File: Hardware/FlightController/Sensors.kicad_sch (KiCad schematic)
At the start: 0 parts

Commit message: Add ICM-42670-P symbol and schematic
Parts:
- added C18: 10nF, Capacitor_SMD:C_0603_1608Metric, symbol Device:C_Small
- added C19: 0.1uF, Capacitor_SMD:C_0603_1608Metric, symbol Device:C_Small
- added C20: 2.2uF, Capacitor_SMD:C_0603_1608Metric, symbol Device:C_Small
- added U4: ICM-42670-P, Package_LGA:LGA-14_3x2.5mm_P0.5mm_LayoutBorder3x4y, symbol FlightControllerLibrary:ICM-42670-P
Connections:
- new net +3V3: C18.1, C19.1, C20.1, U4.12 (AP_CS), U4.5 (VDDIO), U4.8 (VDD)
- new net GND: C18.2, C19.2, C20.2, U4.6 (GND)
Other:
- note added: "IMU"
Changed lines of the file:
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@@
 (kicad_sch (version 20211123) (generator eeschema)
   (paper "A4")
+  (junction (at 90.17 55.88) (diameter 0) (color 0 0 0 0)
+  )
+  (junction (at 77.47 55.88) (diameter 0) (color 0 0 0 0)
+  )
+  (wire (pts (xy 35.56 76.2) (xy 35.56 80.01))
+    (stroke (width 0) (type default) (color 0 0 0 0))
+  )
+  (polyline (pts (xy 16.51 22.86) (xy 110.49 22.86))
+    (stroke (width 0) (type default) (color 0 0 0 0))
+  )
+  (wire (pts (xy 22.86 67.31) (xy 35.56 67.31))
+    (stroke (width 0) (type default) (color 0 0 0 0))
+  )
+  (wire (pts (xy 72.39 55.88) (xy 77.47 55.88))
+    (stroke (width 0) (type default) (color 0 0 0 0))
+  )
+  (wire (pts (xy 77.47 55.88) (xy 90.17 55.88))
+    (stroke (width 0) (type default) (color 0 0 0 0))
+  )
+  (wire (pts (xy 90.17 55.88) (xy 97.79 55.88))
+    (stroke (width 0) (type default) (color 0 0 0 0))
+  )
+  (polyline (pts (xy 110.49 22.86) (xy 110.49 87.63))
+    (stroke (width 0) (type default) (color 0 0 0 0))
+  )
+  (wire (pts (xy 35.56 67.31) (xy 35.56 71.12))
+    (stroke (width 0) (type default) (color 0 0 0 0))
+  )
+  (polyline (pts (xy 16.51 87.63) (xy 16.51 22.86))
+    (stroke (width 0) (type default) (color 0 0 0 0))
+  )
+  (polyline (pts (xy 110.49 87.63) (xy 16.51 87.63))
+    (stroke (width 0) (type default) (color 0 0 0 0))
+  )
+  (text "IMU" (at 58.42 21.59 0)
+    (effects (font (size 1.27 1.27) (thickness 0.254) bold) (justify left bottom))
+  )
+  (global_label "ACCEL_VDDIO" (shape input) (at 60.96 40.64 90) (fields_autoplaced)
+    (effects (font (size 1.27 1.27)) (justify left))
+    (property "Intersheet References" "${INTERSHEET_REFS}" (id 0) (at 61.0394 25.8898 90)
+      (effects (font (size 1.27 1.27)) (justify left) hide)
+    )
+  )
+  (global_label "ACCEL_VDDIO" (shape input) (at 35.56 67.31 0) (fields_autoplaced)
+    (effects (font (size 1.27 1.27)) (justify left))
+    (property "Intersheet References" "${INTERSHEET_REFS}" (id 0) (at 50.3102 67.3894 0)
+      (effects (font (size 1.27 1.27)) (justify left) hide)
+    )
+  )
+  (global_label "ACCEL_VDDIO" (shape input) (at 55.88 59.69 270) (fields_autoplaced)
+    (effects (font (size 1.27 1.27)) (justify right))
+    (property "Intersheet References" "${INTERSHEET_REFS}" (id 0) (at 55.8006 74.4402 90)
+      (effects (font (size 1.27 1.27)) (justify right) hide)
+    )
+  )
+  (symbol (lib_id "power:GND") (at 90.17 60.96 0) (unit 1)
+    (in_bom yes) (on_board yes) (fields_autoplaced)
+    (property "Reference" "#PWR026" (id 0) (at 90.17 67.31 0)
+      (effects (font (size 1.27 1.27)) hide)
+    )
+    (property "Value" "GND" (id 1) (at 90.17 66.04 0))
+    (property "Footprint" "" (id 2) (at 90.17 60.96 0)
+      (effects (font (size 1.27 1.27)) hide)
+    )
+    (property "Datasheet" "" (id 3) (at 90.17 60.96 0)
+      (effects (font (size 1.27 1.27)) hide)
+    )
+    (pin "1")
+  )
+  (symbol (lib_id "power:GND") (at 77.47 60.96 0) (unit 1)
+    (in_bom yes) (on_board yes) (fields_autoplaced)
+    (property "Reference" "#PWR025" (id 0) (at 77.47 67.31 0)
+      (effects (font (size 1.27 1.27)) hide)
+    )
+    (property "Value" "GND" (id 1) (at 77.47 66.04 0))
+    (property "Footprint" "" (id 2) (at 77.47 60.96 0)
+      (effects (font (size 1.27 1.27)) hide)
+    )
+    (property "Datasheet" "" (id 3) (at 77.47 60.96 0)
+      (effects (font (size 1.27 1.27)) hide)
+    )
+    (pin "1")
+  )
+  (symbol (lib_id "power:GND") (at 35.56 80.01 0) (unit 1)
+    (in_bom yes) (on_board yes) (fields_autoplaced)
+    (property "Reference" "#PWR023" (id 0) (at 35.56 86.36 0)
+      (effects (font (size 1.27 1.27)) hide)
+    )
+    (property "Value" "GND" (id 1) (at 35.56 85.09 0))
+    (property "Footprint" "" (id 2) (at 35.56 80.01 0)
+      (effects (font (size 1.27 1.27)) hide)
+    )
+    (property "Datasheet" "" (id 3) (at 35.56 80.01 0)
+      (effects (font (size 1.27 1.27)) hide)
+    )
+    (pin "1")
+  )
+  (symbol (lib_id "Device:C_Small") (at 35.56 73.66 0) (unit 1)
+    (in_bom yes) (on_board yes) (fields_autoplaced)
+    (property "Reference" "C18" (id 0) (at 38.1 72.3962 0)
+      (effects (font (size 1.27 1.27)) (justify left))
+    )
+    (property "Value" "10nF" (id 1) (at 38.1 74.9362 0)
+      (effects (font (size 1.27 1.27)) (justify left))
+    )
+    (property "Footprint" "Capacitor_SMD:C_0603_1608Metric" (id 2) (at 35.56 73.66 0)
+      (effects (font (size 1.27 1.27)) hide)
+    )
+    (property "Datasheet" "~" (id 3) (at 35.56 73.66 0)
+      (effects (font (size 1.27 1.27)) hide)
+    )
+    (pin "1")
+    (pin "2")
+  )
+  (symbol (lib_id "power:GND") (at 58.42 59.69 0) (unit 1)
+    (in_bom yes) (on_board yes) (fields_autoplaced)
+    (property "Reference" "#PWR024" (id 0) (at 58.42 66.04 0)
+      (effects (font (size 1.27 1.27)) hide)
+    )
+    (property "Value" "GND" (id 1) (at 58.42 64.77 0))
+    (property "Footprint" "" (id 2) (at 58.42 59.69 0)
+      (effects (font (size 1.27 1.27)) hide)
+    )
+    (property "Datasheet" "" (id 3) (at 58.42 59.69 0)
+      (effects (font (size 1.27 1.27)) hide)
+    )
+    (pin "1")
+  )
+  (symbol (lib_id "power:+3.3V") (at 22.86 67.31 90) (unit 1)
+    (in_bom yes) (on_board yes)
+    (property "Reference" "#PWR022" (id 0) (at 26.67 67.31 0)
+      (effects (font (size 1.27 1.27)) hide)
+    )
+    (property "Value" "+3.3V" (id 1) (at 21.59 64.77 90)
+      (effects (font (size 1.27 1.27)) (justify right))
+    )
+    (property "Footprint" "" (id 2) (at 22.86 67.31 0)
+      (effects (font (size 1.27 1.27)) hide)
+    )
+    (property "Datasheet" "" (id 3) (at 22.86 67.31 0)
+      (effects (font (size 1.27 1.27)) hide)
+    )
+    (pin "1")
+  )
+  (symbol (lib_id "Device:C_Small") (at 77.47 58.42 0) (unit 1)
+    (in_bom yes) (on_board yes) (fields_autoplaced)
+    (property "Reference" "C19" (id 0) (at 80.01 57.1562 0)
+      (effects (font (size 1.27 1.27)) (justify left))
+    )
+    (property "Value" "0.1uF" (id 1) (at 80.01 59.6962 0)
+      (effects (font (size 1.27 1.27)) (justify left))
+    )
+    (property "Footprint" "Capacitor_SMD:C_0603_1608Metric" (id 2) (at 77.47 58.42 0)
+      (effects (font (size 1.27 1.27)) hide)
+    )
+    (property "Datasheet" "~" (id 3) (at 77.47 58.42 0)
+      (effects (font (size 1.27 1.27)) hide)
+    )
+    (pin "1")
+    (pin "2")
+  )
+  (symbol (lib_id "FlightControllerLibrary:ICM-42670-P") (at 55.88 48.26 0) (unit 1)
+    (in_bom yes) (on_board yes) (fields_autoplaced)
+    (property "Reference" "U4" (id 0) (at 62.9794 38.1 0)
+      (effects (font (size 1.27 1.27)) (justify left))
+    )
+    (property "Value" "ICM-42670-P" (id 1) (at 62.9794 40.64 0)
+      (effects (font (size 1.27 1.27)) (justify left))
+    )
+    (property "Footprint" "Package_LGA:LGA-14_3x2.5mm_P0.5mm_LayoutBorder3x4y" (id 2) (at 55.88 45.72 0)
+      (effects (font (size 1.27 1.27)) hide)
+    )
+    (property "Datasheet" "" (id 3) (at 55.88 45.72 0)
+      (effects (font (size 1.27 1.27)) hide)
+    )
+    (pin "1")
+    (pin "10")
+    (pin "11")
+    (pin "12")
+    (pin "13")
+    (pin "14")
+    (pin "2")
+    (pin "3")
+    (pin "4")
+    (pin "5")
+    (pin "6")
+    (pin "7")
+    (pin "8")
+    (pin "9")
+  )
+  (symbol (lib_id "Device:C_Small") (at 90.17 58.42 0) (unit 1)
+    (in_bom yes) (on_board yes) (fields_autoplaced)
+    (property "Reference" "C20" (id 0) (at 92.71 57.1562 0)
+      (effects (font (size 1.27 1.27)) (justify left))
+    )
+    (property "Value" "2.2uF" (id 1) (at 92.71 59.6962 0)
+      (effects (font (size 1.27 1.27)) (justify left))
+    )
+    (property "Footprint" "Capacitor_SMD:C_0603_1608Metric" (id 2) (at 90.17 58.42 0)
+      (effects (font (size 1.27 1.27)) hide)
+    )
+    (property "Datasheet" "~" (id 3) (at 90.17 58.42 0)
+      (effects (font (size 1.27 1.27)) hide)
+    )
+    (pin "1")
+    (pin "2")
+  )
+  (symbol (lib_id "power:+3.3V") (at 97.79 55.88 270) (unit 1)
+    (in_bom yes) (on_board yes) (fields_autoplaced)
+    (property "Reference" "#PWR027" (id 0) (at 93.98 55.88 0)
+      (effects (font (size 1.27 1.27)) hide)
+    )
+    (property "Value" "+3.3V" (id 1) (at 101.6 55.8799 90)
+      (effects (font (size 1.27 1.27)) (justify left))
+    )
+    (property "Footprint" "" (id 2) (at 97.79 55.88 0)
+      (effects (font (size 1.27 1.27)) hide)
+    )
+    (property "Datasheet" "" (id 3) (at 97.79 55.88 0)
+      (effects (font (size 1.27 1.27)) hide)
+    )
+    (pin "1")
+  )
 )

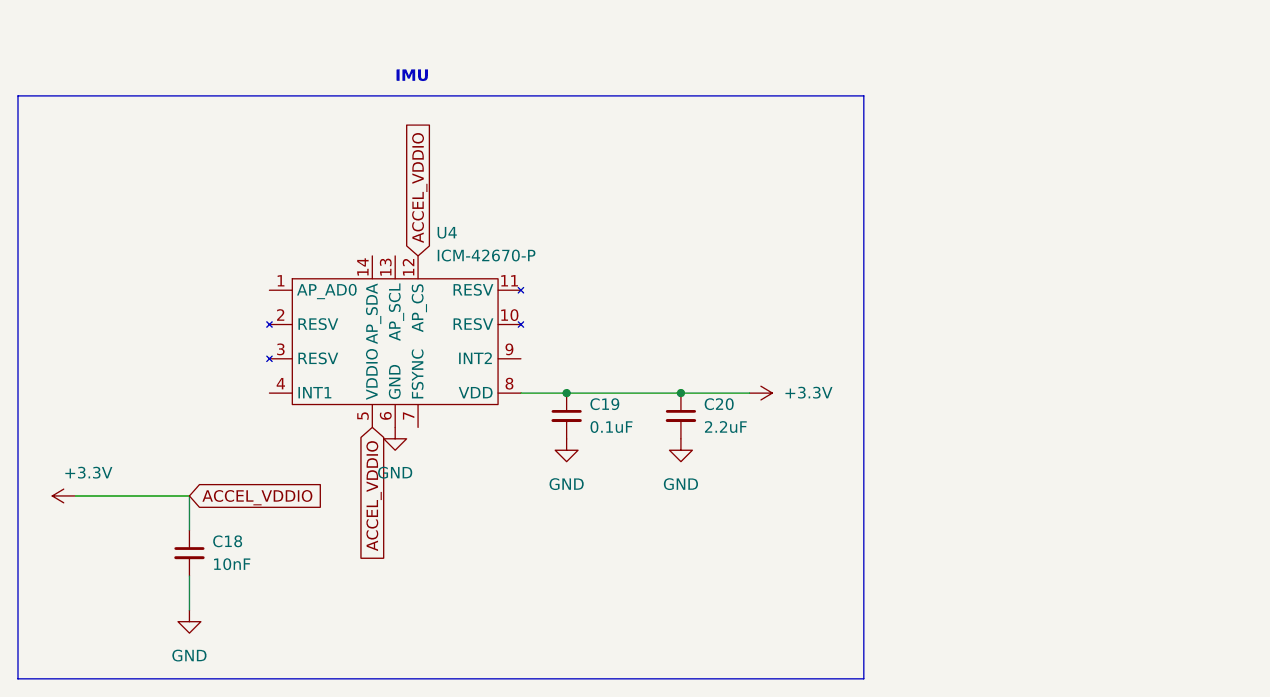
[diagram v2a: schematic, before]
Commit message: Round out basic schematic and add preliminary board layout
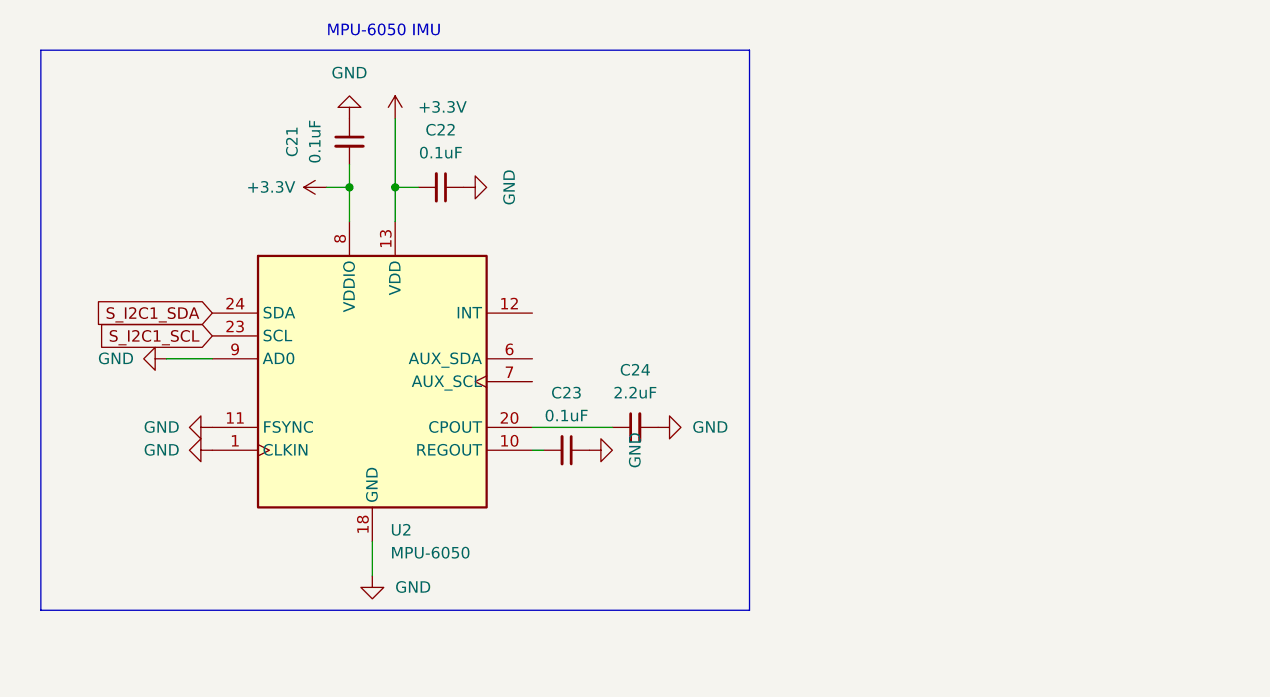
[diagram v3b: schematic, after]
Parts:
- removed C18: 10nF, Capacitor_SMD:C_0603_1608Metric, symbol Device:C_Small
- removed C19: 0.1uF, Capacitor_SMD:C_0603_1608Metric, symbol Device:C_Small
- removed C20: 2.2uF, Capacitor_SMD:C_0603_1608Metric, symbol Device:C_Small
- removed U4: ICM-42670-P, Package_LGA:LGA-14_3x2.5mm_P0.5mm_LayoutBorder3x4y, symbol FlightControllerLibrary:ICM-42670-P
- added C21, C22, C23: 0.1uF, Capacitor_SMD:C_0402_1005Metric, symbol Device:C_Small
- added C24: 2.2uF, Capacitor_SMD:C_0402_1005Metric, symbol Device:C_Small
- added U2: MPU-6050, Sensor_Motion:InvenSense_QFN-24_4x4mm_P0.5mm, symbol Sensor_Motion:MPU-6050
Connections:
- net +3V3: now also C21.2, C22.2, U2.13 (VDD), U2.8 (VDDIO)
- net GND: now also C21.1, C22.1, C23.1, C24.2, U2.1 (CLKIN), U2.11 (FSYNC), U2.18 (GND), U2.9 (AD0)
- new net: C24.1, U2.20 (CPOUT)
- new net: C23.2, U2.10 (REGOUT)
- new net S_I2C1_SCL: U2.23 (SCL)
- new net S_I2C1_SDA: U2.24 (SDA)
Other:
- note added: "MPU-6050 IMU"
- note removed: "IMU"

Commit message: Add and route SBUS inverter
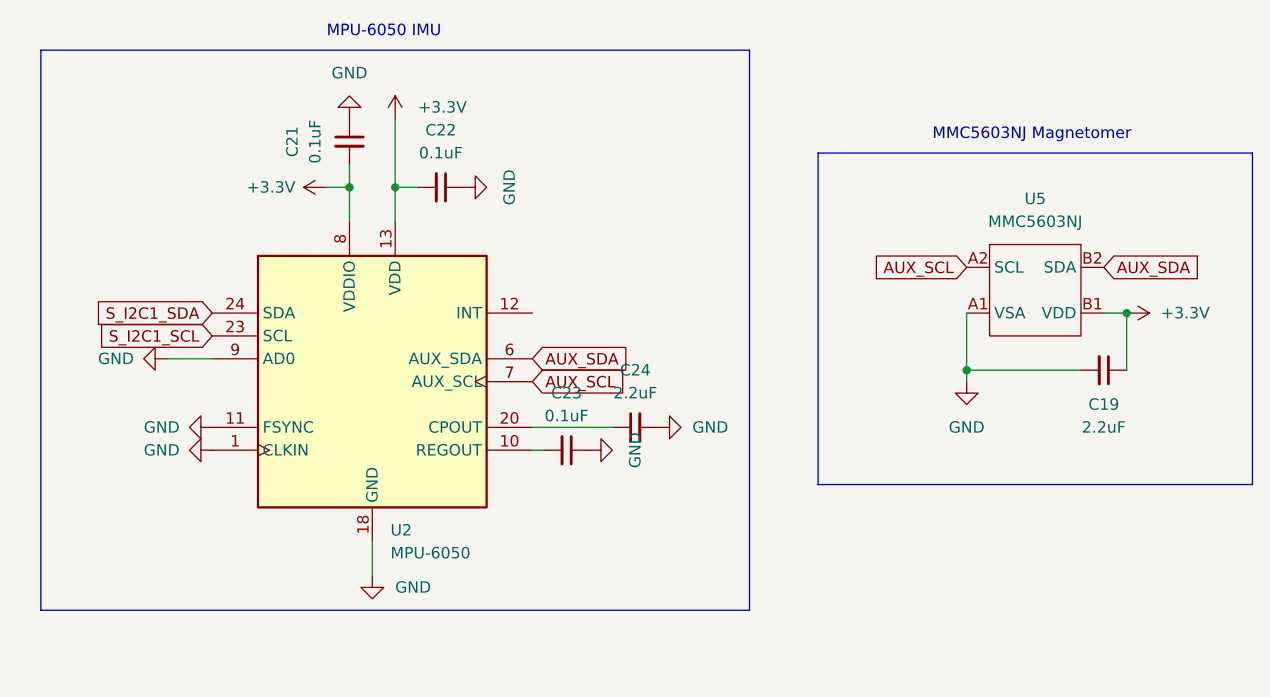
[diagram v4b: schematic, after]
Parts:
- added C19: 2.2uF, Capacitor_SMD:C_0402_1005Metric, symbol Device:C_Small
- added U5: MMC5603NJ, Package_BGA:WLP-4_0.83x0.83mm_P0.4mm, symbol FlightControllerLibrary:MMC5603NJ
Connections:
- net +3V3: now also C19.1, U5.B1 (VDD)
- net GND: now also C19.2, U5.A1 (VSA)
- net AUX_SDA: now reaches U2.6 (AUX_SDA)
- net AUX_SDA: now also U5.B2 (SDA)
- net AUX_SCL: now reaches U2.7 (AUX_SCL)
- net AUX_SCL: now also U5.A2 (SCL)
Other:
- note added: "MMC5603NJ Magnetomer"
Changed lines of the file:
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@@
   (junction (at 58.42 33.02) (diameter 0) (color 0 0 0 0)
   )
+  (junction (at 121.92 53.34) (diameter 0) (color 0 0 0 0)
+  )
   (junction (at 53.34 33.02) (diameter 0) (color 0 0 0 0)
   )
+  (junction (at 139.7 46.99) (diameter 0) (color 0 0 0 0)
+  )
   (polyline (pts (xy 19.05 80.01) (xy 19.05 17.78))
     (stroke (width 0) (type default) (color 0 0 0 0))
@@
     (stroke (width 0) (type default) (color 0 0 0 0))
   )
+  (wire (pts (xy 121.92 53.34) (xy 134.62 53.34))
+    (stroke (width 0) (type default) (color 0 0 0 0))
+  )
+  (polyline (pts (xy 153.67 66.04) (xy 105.41 66.04))
+    (stroke (width 0) (type default) (color 0 0 0 0))
+  )
+  (polyline (pts (xy 105.41 66.04) (xy 105.41 29.21))
+    (stroke (width 0) (type default) (color 0 0 0 0))
+  )
   (wire (pts (xy 53.34 33.02) (xy 53.34 36.83))
     (stroke (width 0) (type default) (color 0 0 0 0))
   )
+  (wire (pts (xy 137.16 46.99) (xy 139.7 46.99))
+    (stroke (width 0) (type default) (color 0 0 0 0))
+  )
   (wire (pts (xy 55.88 76.2) (xy 55.88 72.39))
     (stroke (width 0) (type default) (color 0 0 0 0))
@@
     (stroke (width 0) (type default) (color 0 0 0 0))
   )
+  (wire (pts (xy 121.92 53.34) (xy 121.92 54.61))
+    (stroke (width 0) (type default) (color 0 0 0 0))
+  )
   (polyline (pts (xy 97.79 80.01) (xy 19.05 80.01))
     (stroke (width 0) (type default) (color 0 0 0 0))
   )
+  (polyline (pts (xy 153.67 29.21) (xy 153.67 66.04))
+    (stroke (width 0) (type default) (color 0 0 0 0))
+  )
+  (wire (pts (xy 139.7 46.99) (xy 139.7 53.34))
+    (stroke (width 0) (type default) (color 0 0 0 0))
+  )
   (wire (pts (xy 58.42 33.02) (xy 58.42 36.83))
     (stroke (width 0) (type default) (color 0 0 0 0))
   )
+  (wire (pts (xy 121.92 46.99) (xy 121.92 53.34))
+    (stroke (width 0) (type default) (color 0 0 0 0))
+  )
   (polyline (pts (xy 97.79 17.78) (xy 97.79 80.01))
     (stroke (width 0) (type default) (color 0 0 0 0))
@@
     (stroke (width 0) (type default) (color 0 0 0 0))
   )
+  (polyline (pts (xy 105.41 29.21) (xy 153.67 29.21))
+    (stroke (width 0) (type default) (color 0 0 0 0))
+  )
   (text "MPU-6050 IMU" (at 50.8 16.51 0)
+    (effects (font (size 1.27 1.27)) (justify left bottom))
+  )
+  (text "MMC5603NJ Magnetomer" (at 118.11 27.94 0)
     (effects (font (size 1.27 1.27)) (justify left bottom))
   )
@@
     )
   )
+  (global_label "AUX_SCL" (shape input) (at 73.66 54.61 0) (fields_autoplaced)
+    (effects (font (size 1.27 1.27)) (justify left))
+    (property "Intersheet References" "${INTERSHEET_REFS}" (id 0) (at 84.1769 54.6894 0)
+      (effects (font (size 1.27 1.27)) (justify left) hide)
+    )
+  )
+  (global_label "AUX_SDA" (shape input) (at 137.16 41.91 0) (fields_autoplaced)
+    (effects (font (size 1.27 1.27)) (justify left))
+    (property "Intersheet References" "${INTERSHEET_REFS}" (id 0) (at 147.7374 41.8306 0)
+      (effects (font (size 1.27 1.27)) (justify left) hide)
+    )
+  )
+  (global_label "AUX_SCL" (shape input) (at 121.92 41.91 180) (fields_autoplaced)
+    (effects (font (size 1.27 1.27)) (justify right))
+    (property "Intersheet References" "${INTERSHEET_REFS}" (id 0) (at 111.4031 41.8306 0)
+      (effects (font (size 1.27 1.27)) (justify right) hide)
+    )
+  )
+  (global_label "AUX_SDA" (shape input) (at 73.66 52.07 0) (fields_autoplaced)
+    (effects (font (size 1.27 1.27)) (justify left))
+    (property "Intersheet References" "${INTERSHEET_REFS}" (id 0) (at 84.2374 51.9906 0)
+      (effects (font (size 1.27 1.27)) (justify left) hide)
+    )
+  )
   (symbol (lib_id "power:+3.3V") (at 58.42 25.4 0) (unit 1)
     (in_bom yes) (on_board yes) (fields_autoplaced)
@@
     )
     (property "Datasheet" "" (id 3) (at 58.42 25.4 0)
+      (effects (font (size 1.27 1.27)) hide)
+    )
+    (pin "1")
+  )
+  (symbol (lib_id "power:+3.3V") (at 139.7 46.99 270) (unit 1)
+    (in_bom yes) (on_board yes) (fields_autoplaced)
+    (property "Reference" "#PWR023" (id 0) (at 135.89 46.99 0)
+      (effects (font (size 1.27 1.27)) hide)
+    )
+    (property "Value" "+3.3V" (id 1) (at 143.51 46.9899 90)
+      (effects (font (size 1.27 1.27)) (justify left))
+    )
+    (property "Footprint" "" (id 2) (at 139.7 46.99 0)
+      (effects (font (size 1.27 1.27)) hide)
+    )
+    (property "Datasheet" "" (id 3) (at 139.7 46.99 0)
       (effects (font (size 1.27 1.27)) hide)
     )
@@
     (pin "2")
   )
+  (symbol (lib_id "Device:C_Small") (at 137.16 53.34 270) (unit 1)
+    (in_bom yes) (on_board yes)
+    (property "Reference" "C19" (id 0) (at 137.16 57.15 90))
+    (property "Value" "2.2uF" (id 1) (at 137.16 59.69 90))
+    (property "Footprint" "Capacitor_SMD:C_0402_1005Metric" (id 2) (at 137.16 53.34 0)
+      (effects (font (size 1.27 1.27)) hide)
+    )
+    (property "Datasheet" "~" (id 3) (at 137.16 53.34 0)
+      (effects (font (size 1.27 1.27)) hide)
+    )
+    (pin "1")
+    (pin "2")
+  )
   (symbol (lib_id "Device:C_Small") (at 63.5 33.02 270) (unit 1)
     (in_bom yes) (on_board yes) (fields_autoplaced)
@@
     (pin "2")
   )
+  (symbol (lib_id "FlightControllerLibrary:MMC5603NJ") (at 129.54 44.45 0) (unit 1)
+    (in_bom yes) (on_board yes) (fields_autoplaced)
+    (property "Reference" "U5" (id 0) (at 129.54 34.29 0))
+    (property "Value" "MMC5603NJ" (id 1) (at 129.54 36.83 0))
+    (property "Footprint" "Package_BGA:WLP-4_0.83x0.83mm_P0.4mm" (id 2) (at 129.54 44.45 0)
+      (effects (font (size 1.27 1.27)) hide)
+    )
+    (property "Datasheet" "" (id 3) (at 129.54 44.45 0)
+      (effects (font (size 1.27 1.27)) hide)
+    )
+    (pin "A1")
+    (pin "A2")
+    (pin "B1")
+    (pin "B2")
+  )
   (symbol (lib_id "Device:C_Small") (at 53.34 27.94 0) (unit 1)
     (in_bom yes) (on_board yes) (fields_autoplaced)
@@
       (effects (font (size 1.27 1.27)) hide)
     )
+    (pin "1")
+  )
+  (symbol (lib_id "power:GND") (at 121.92 54.61 0) (unit 1)
+    (in_bom yes) (on_board yes) (fields_autoplaced)
+    (property "Reference" "#PWR022" (id 0) (at 121.92 60.96 0)
+      (effects (font (size 1.27 1.27)) hide)
+    )
+    (property "Value" "GND" (id 1) (at 121.92 59.69 0))
+    (property "Footprint" "" (id 2) (at 121.92 54.61 0)
+      (effects (font (size 1.27 1.27)) hide)
+    )
+    (property "Datasheet" "" (id 3) (at 121.92 54.61 0)
+      (effects (font (size 1.27 1.27)) hide)
+    )
